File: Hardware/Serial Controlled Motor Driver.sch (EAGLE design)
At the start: 43 parts, among them J1 DNP, J2 DNP, J3 DNP, J4 DNP, J5 DNP, J6 DNP, J7 DNP, U1 CY8C4245LQI-483, U2 DRV8835

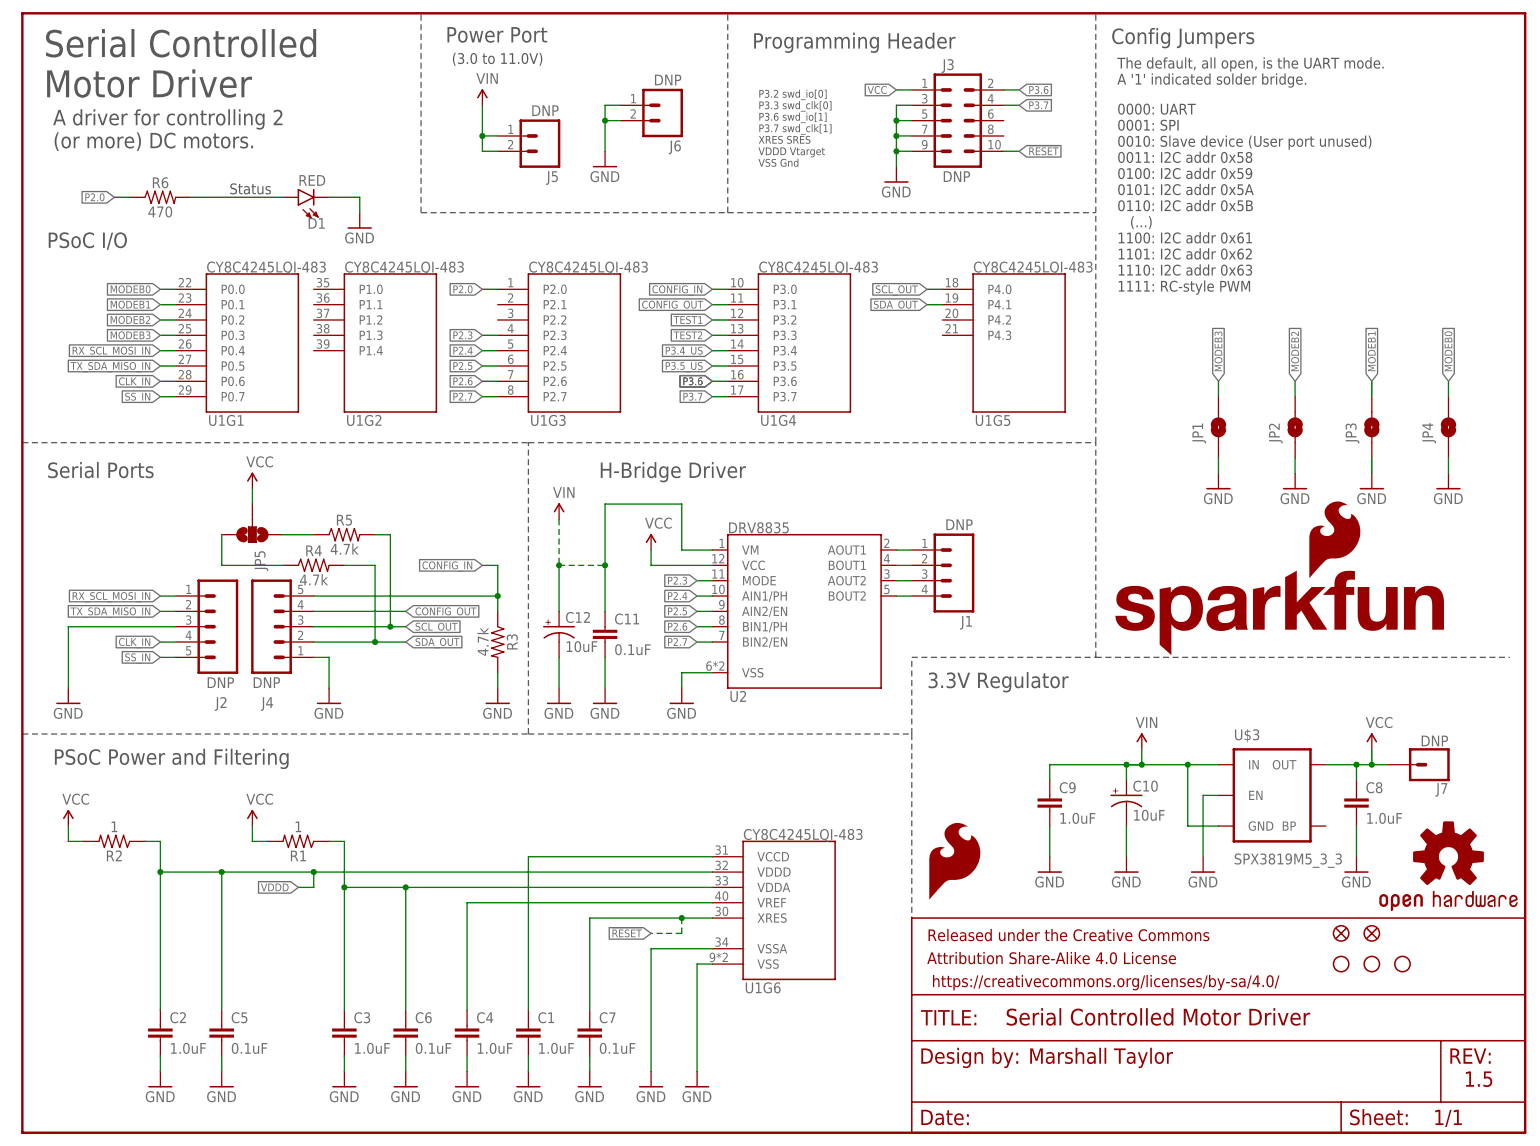
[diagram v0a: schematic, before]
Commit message: Bringing branch up to date with current design work while tracking only necessary PSoC build files
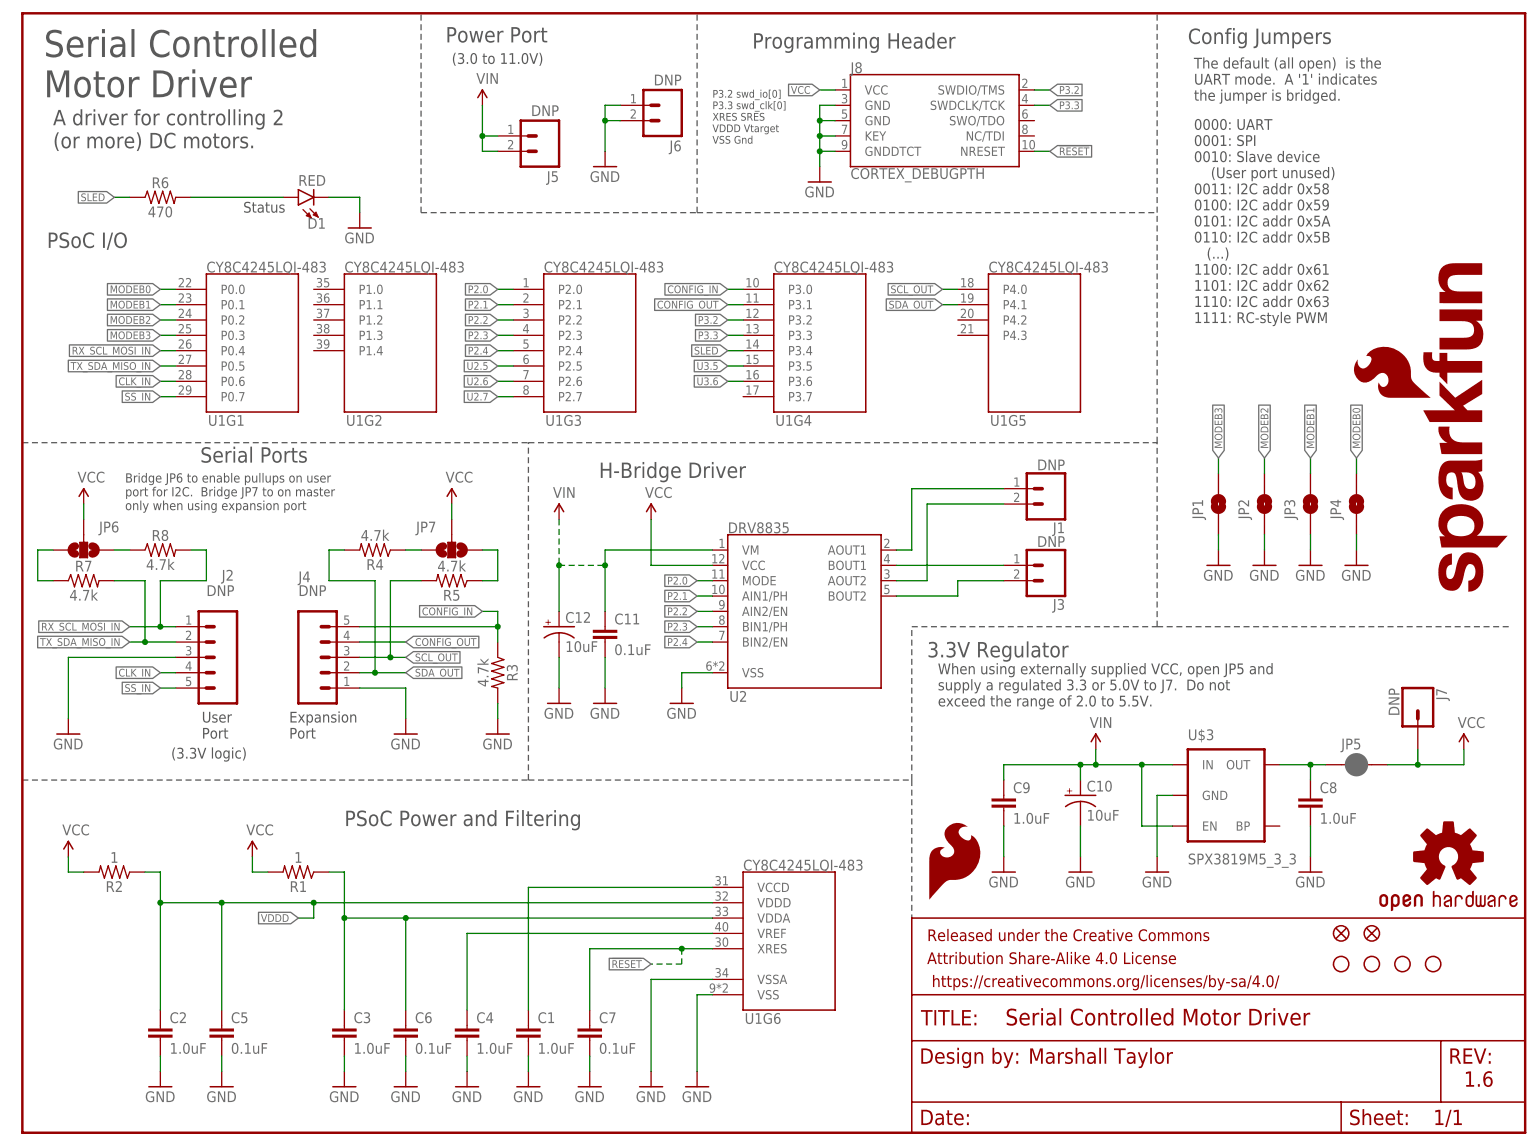
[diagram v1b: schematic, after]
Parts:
- added H4: STAND-OFF, SparkFun-Electromechanical:STAND-OFF
- added J8: CORTEX_DEBUGPTH, Pete_Connectors_Retired:CORTEX_DEBUGPTH
- added JP6, JP7: JUMPER-PAD-3-NOYES_SILK, SparkFun-Passives:JUMPER-PAD-3-NOYES_SILK
- added R7, R8: 4.7k, SparkFun-Resistors:4.7KOHM-0603-1/10W-1%
- J1: device SparkFun-Connectors:M04PTH -> SparkFun-Connectors:CONN_021X02_NO_SILK
- J3: device SparkFun-Connectors:M05X20.05_IN_PTH_SILK -> SparkFun-Connectors:CONN_021X02_NO_SILK
- JP5: value JUMPER-PAD-3-NOYES_SILK -> JUMPER-PAD-2; device SparkFun-Passives:JUMPER-PAD-3-NOYES_SILK -> SparkFun-Jumpers:JUMPER-PAD-2-NC_BY_PASTE
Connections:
- net N$5 renamed AOUT1
- net P3.5_US renamed U3.5
- removed net N$7: J1.4, U2.BOUT2
- removed net N$8: J1.3, U2.AOUT2
- removed net N$9: JP5.3, R4.1
- removed net P2.5: U1G3.P2.5, U2.AIN2/EN
- removed net P2.6: U1G3.P2.6, U2.BIN1/PH
- removed net P2.7: U1G3.P2.7, U2.BIN2/EN
- removed net P3.4_US: U1G4.P3.4
- removed net P3.6: J3.2, U1G4.P3.6
- removed net P3.7: J3.4, U1G4.P3.7
- removed net TEST1: U1G4.P3.2
- removed net TEST2: U1G4.P3.3
- new net AOUT2: J1.2, U2.AOUT2
- new net BOUT1: J3.1, U2.BOUT1
- new net BOUT2: J3.2, U2.BOUT2
- new net N$11: JP6.1, R8.1
- new net N$12: JP6.3, R7.1
- new net N$5: C8.1, JP5.1, U$3.OUT
- new net P2.1: U1G3.P2.1, U2.AIN1/PH
- new net P2.2: U1G3.P2.2, U2.AIN2/EN
- new net P3.2: J8.SWDIO/TMS, U1G4.P3.2
- new net P3.3: J8.SWDCLK/TCK, U1G4.P3.3
- new net SLED: R6.1, U1G4.P3.4
- new net U2.5: U1G3.P2.5
- new net U2.6: U1G3.P2.6
- new net U2.7: U1G3.P2.7
- new net U3.6: U1G4.P3.6
- net !RESET: now also J8.NRESET; no longer J3.10
- net GND: now also J8.GND@3, J8.GND@5, J8.GNDDTCT, J8.KEY, U$3.GND; no longer J3.3, J3.5, J3.7, J3.9, U$3.EN
- net N$2: now also JP7.1, R4.1; no longer JP5.1, R5.1
- net N$6: now also JP7.3, R5.1; no longer J1.2, U2.BOUT1
- net P2.0: now also U2.MODE; no longer R6.1
- net P2.3: now also U2.BIN1/PH; no longer U2.MODE
- net P2.4: now also U2.BIN2/EN; no longer U2.AIN1/PH
- net RX_SCL_MOSI_IN: now also R8.2
- net TX_SDA_MISO_IN: now also R7.2
- net VCC: now also J8.VCC, JP6.2, JP7.2; no longer C8.1, J3.1, U$3.OUT
- net VIN: now also U$3.EN; no longer U$3.GND
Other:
- note added: "(3.3V logic)"
- note added: "1.6"
- note added: "Bridge JP6 to enable pullups on user port for I2C. Bridge JP7 to on master only when using expansion port"
- note added: "Expansion Port"
- note added: "P3.2 swd_io[0] P3.3 swd_clk[0] XRES SRES VDDD Vtarget VSS Gnd"
- note added: "The default (all open) is the UART mode. A '1' indicates the jumper is bridged."
- note added: "User Port"
- note added: "When using externally supplied VCC, open JP5 and supply a regulated 3.3 or 5.0V to J7. Do not exceed the range of 2.0 to 5.5V."
- note removed: "1.5"
- note removed: "P3.2 swd_io[0] P3.3 swd_clk[0] P3.6 swd_io[1] P3.7 swd_clk[1] XRES SRES VDDD Vtarget VSS Gnd"
- note removed: "The default, all open, is the UART mode. A '1' indicated solder bridge."
- moved on the sheet: C10, C8, C9, J2, J4, J7, JP1, JP2, JP3, JP4, R1, R2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

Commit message: Incremented version numbers in eagle files
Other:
- note added: "1.6.1"
- note removed: "1.6"
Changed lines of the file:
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@@
 <wire x1="83.82" y1="114.3" x2="187.96" y2="114.3" width="0.1524" layer="97" style="longdash"/>
 <text x="149.86" y="78.74" size="2.54" layer="97" font="vector" ratio="15">3.3V Regulator</text>
-<text x="238.76" y="7.62" size="2.54" layer="94" font="vector">1.6</text>
+<text x="237.49" y="7.62" size="2.54" layer="94" font="vector">1.6.1</text>
 <text x="114.3" y="172.72" size="1.27" layer="97" rot="MR180">P3.2 swd_io[0]
 P3.3 swd_clk[0]

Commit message: Fixed proto errors and started final API for arduino
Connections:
- net CONFIG_IN: now also J4.4, U1G4.P3.1; no longer J4.5, R3.1, U1G4.P3.0
- net CONFIG_OUT: now also J4.5, R3.1, U1G4.P3.0; no longer J4.4, U1G4.P3.1
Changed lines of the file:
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@@
 </segment>
 </net>
-<net name="CONFIG_OUT" class="0">
+<net name="CONFIG_IN" class="0">
 <segment>
 <wire x1="55.88" y1="81.28" x2="63.5" y2="81.28" width="0.1524" layer="91"/>
@@
 </segment>
 </net>
-<net name="CONFIG_IN" class="0">
+<net name="CONFIG_OUT" class="0">
 <segment>
 <wire x1="55.88" y1="83.82" x2="78.74" y2="83.82" width="0.1524" layer="91"/>

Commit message: Added Byron's review suggestions
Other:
- note added: "2.0"
- note added: "Open JP5 to disconnect 3.3V regulated supply. In this configuration, a regulated voltage must be attached to the VCC pin, and must be in the range of 2.0 to 5.5V."
- note removed: "1.6.1"
- note removed: "When using externally supplied VCC, open JP5 and supply a regulated 3.3 or 5.0V to J7. Do not exceed the range of 2.0 to 5.5V."
